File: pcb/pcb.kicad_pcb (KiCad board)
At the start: 2 copper layers, 61 x 81 mm, 50 parts, among them J1 LEFT, J2 LEFT-EXT, J3 RIGHT, J4 RIGHT-EXT, J5 EXT POWER, J6 RJ45, J7 RJ45, SW1 Reset, SW2 Factory Reset, SW3 User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

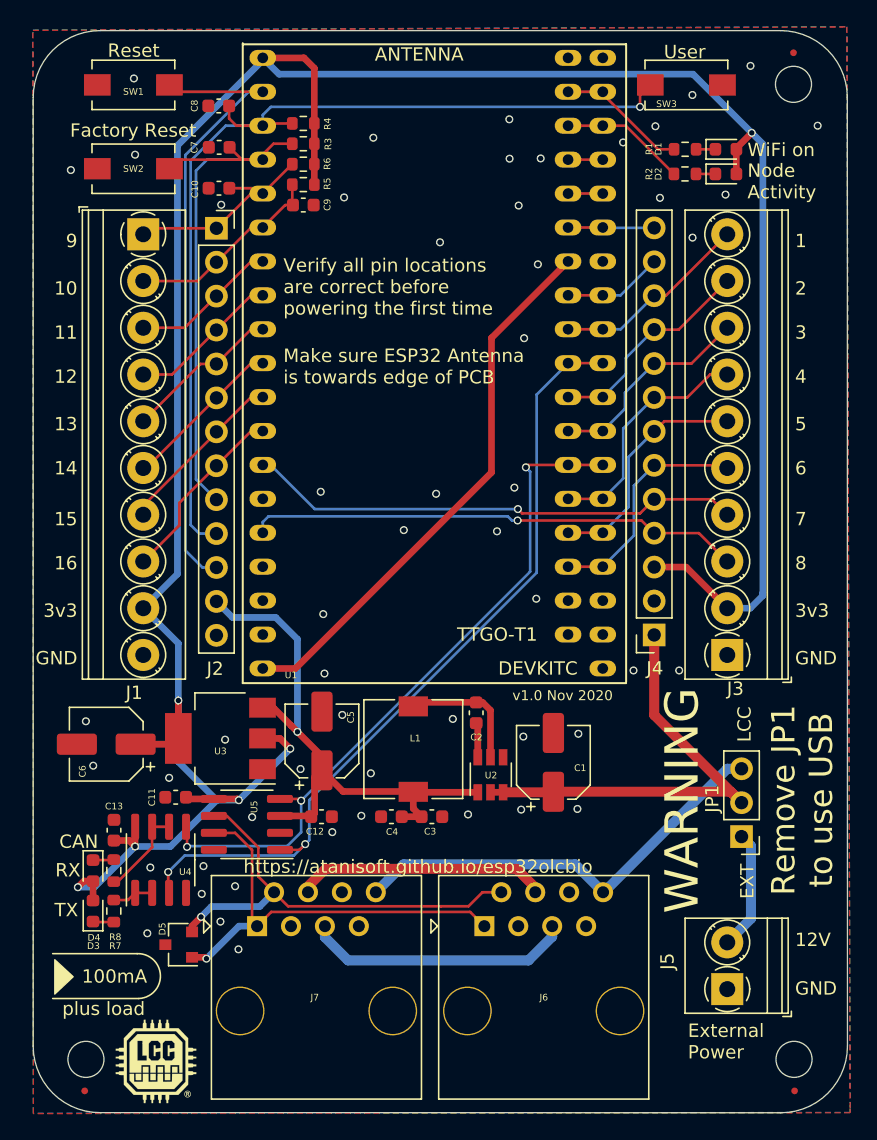
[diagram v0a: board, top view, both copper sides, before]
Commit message: PCA9685 support (#9)
* Sync PWM changes

* bump build to IDF v4.4

* Bump dependencies

* refresh web interface for new servo config

* Fix https://github.com/atanisoft/Esp32OlcbIO/issues/8

* PCB updates for KiCad6

* IO PCB v1.1

Spaced out RJ45 jacks to provide easier access to USB connector.

Fixes: https://github.com/atanisoft/Esp32OlcbIO/issues/3

* drop old project files

* Adding one additional GND via to v1.1 PCB, add position file.

* Migrate to IDF component manager
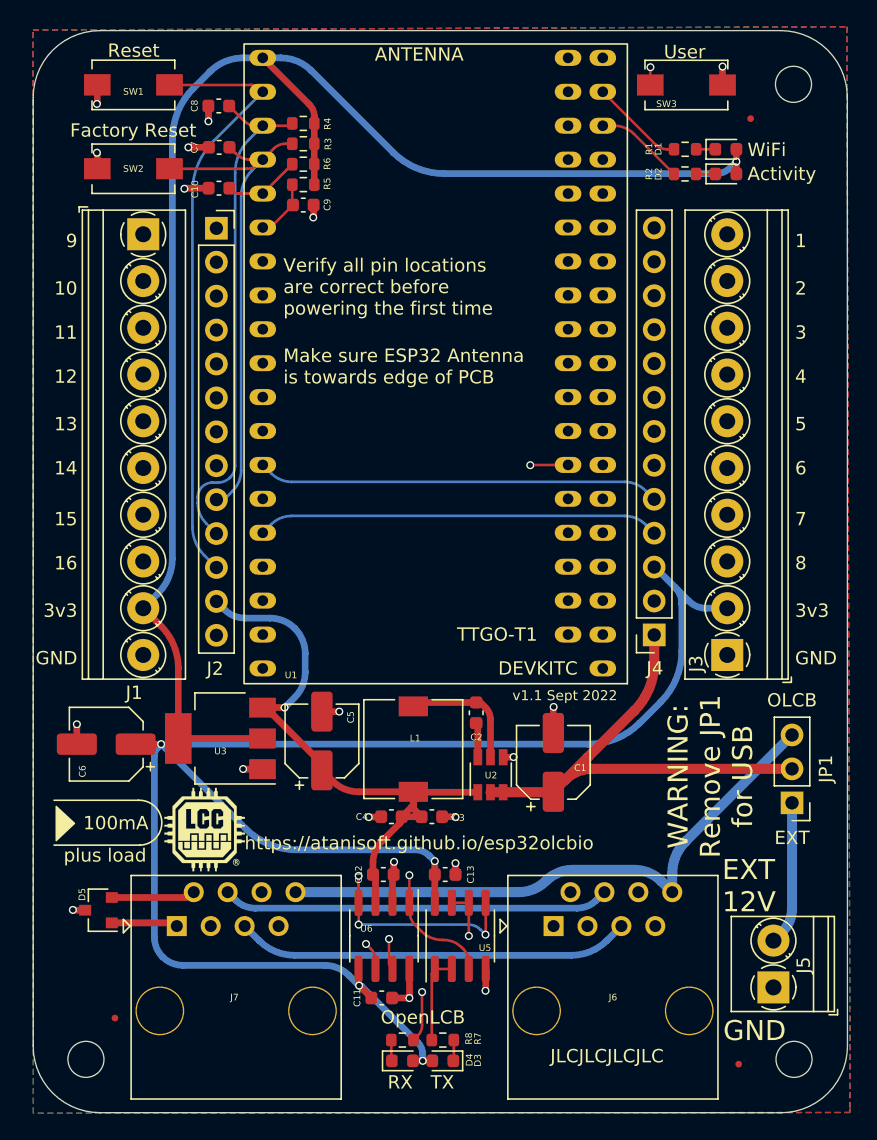
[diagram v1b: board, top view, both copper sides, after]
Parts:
- added REF**: OSHW-Logo2_7.3x6mm_SilkScreen, Symbol:OSHW-Logo2_7.3x6mm_SilkScreen, B.Cu at (136.9, 64.8)
- added REF**: KiCad-Logo2_5mm_SilkScreen, Symbol:KiCad-Logo2_5mm_SilkScreen, B.Cu at (137.0, 58.6)
- moved D3 28.5 mm to (137.4, 125.4), turned to 180 degrees
- moved D4 27.2 mm to (134.3, 125.4), turned to 0 degrees
- moved R7 26.5 mm to (137.4, 123.8), turned to 0 degrees
- moved R8 25.1 mm to (134.3, 123.8), turned to 180 degrees
- moved C13 25.0 mm to (137.5, 111.5), turned to 180 degrees
- moved U5 23.2 mm to (138.7, 116.0)
- moved C11 21.5 mm to (132.8, 120.7), turned to 0 degrees
- moved G*** 17.7 mm to (119.5, 108.0)
- moved U6 13.2 mm to (132.9, 116.0), turned to -90 degrees
- moved D5 6.54 mm to (111.6, 114.1)
- moved C12 6.34 mm to (132.9, 111.5)
- moved J7 6.01 mm to (117.4, 115.3)
- moved FID2 5.90 mm to (112.8, 122.2)
- moved FID1 5.88 mm to (160.4, 54.9)
- moved J6 5.18 mm to (145.6, 115.3)
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- renumbered U4 to U5, U5 to U6
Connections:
- U1 pad 1: Net-(U1-Pad1) -> unconnected-(U1-Pad1)
- U1 pad 3: Net-(U1-Pad3) -> unconnected-(U1-Pad3)
- U1 pad 5V: Net-(U1-Pad5V) -> unconnected-(U1-Pad5V)
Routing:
- net +3V3: track 200.7 -> 243.9 mm, vias 6 -> 5
- net Net-(U1-Pad5V): track 41.4 -> 0.00 mm
- net GND: track 0.00 -> 28.4 mm, vias 54 -> 19
- net VDDA: track 32.9 -> 44.5 mm
- net ALT-A: track 18.9 -> 29.0 mm
- net ALT-B: track 20.1 -> 29.7 mm
- net CAN-L: track 33.7 -> 41.5 mm
- net CAN-TX: track 61.6 -> 54.8 mm, vias 2 -> 1
- net Net-(R8-Pad1): track 6.74 -> 13.2 mm, vias 0 -> 2
- net CAN-RX: track 52.6 -> 57.0 mm, vias 3 -> 4
- net CAN-H: track 33.1 -> 37.3 mm
- net FACTORY_RESET: track 43.7 -> 39.6 mm
- net Net-(R7-Pad1): track 3.09 -> 6.65 mm
- net VCC: track 34.4 -> 37.7 mm
- net +5V: track 43.3 -> 46.1 mm
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- added copper zone on In1.Cu, net GND
- added copper zone on In2.Cu, net GND
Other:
- copper layers 2 -> 4
- net class Default removed
- board text added: "Activity"
- board text added: "EXT 12V"
- board text added: "OLCB"
- board text added: "OpenLCB"
- board text added: "WARNING: Remove JP1 for USB"
- board text added: "WiFi"
- board text added: "v1.1 Sept 2022"
- board text added: "v1.1 September 2022"
- board text removed: "12V"
- board text removed: "CAN"
- board text removed: "External Power"
- board text removed: "LCC"
- board text removed: "Node Activity"
- board text removed: "Remove JP1 to use USB"
- board text removed: "WARNING"
- board text removed: "WiFi on"
- board text removed: "v1.0 Nov 2020"
- board text removed: "v1.0 November 2020"
